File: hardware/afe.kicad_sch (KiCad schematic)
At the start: 36 parts, among them J2 Conn_01x02_Pin, U2 MCP6002-xMC, U3 4052

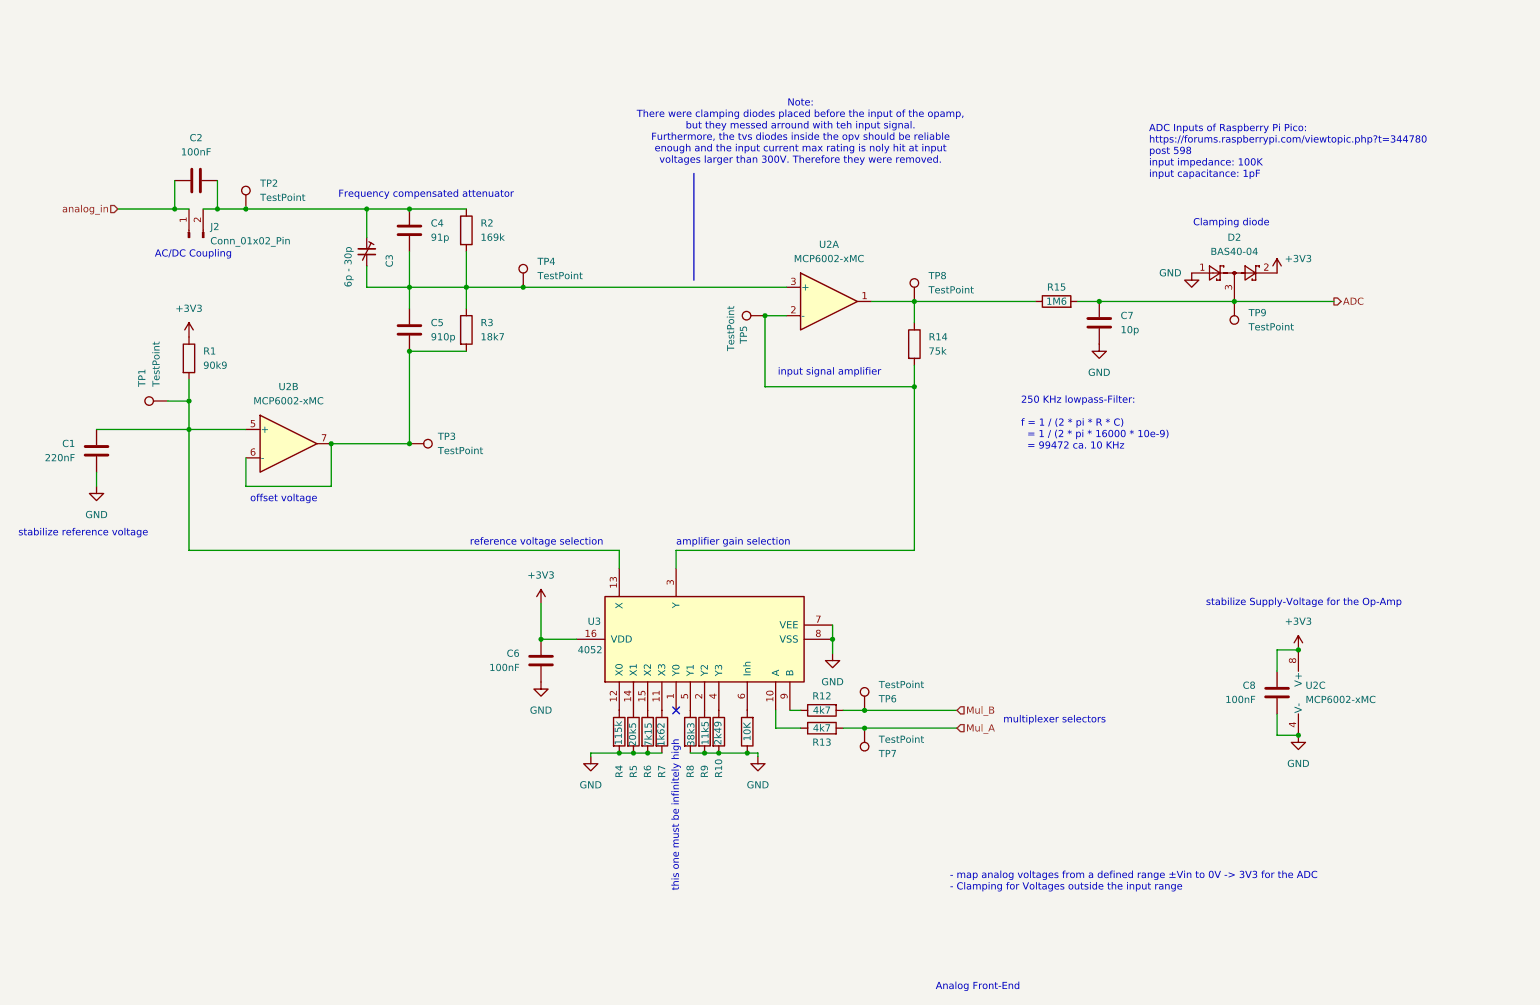
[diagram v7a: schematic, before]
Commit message: remove clamping diodes completely
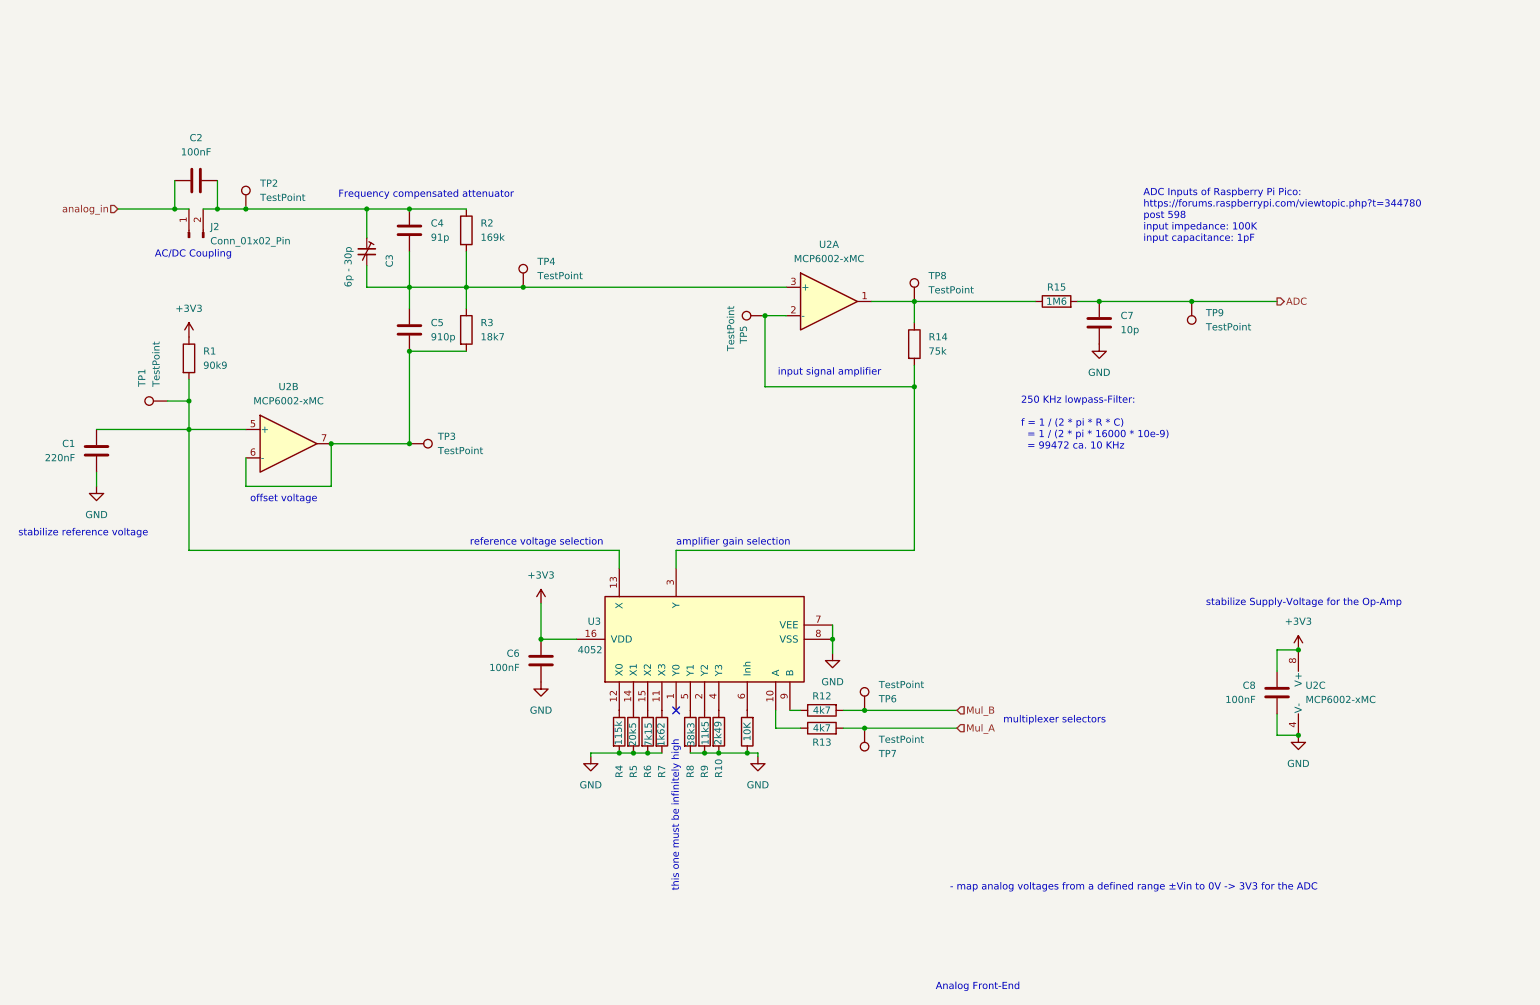
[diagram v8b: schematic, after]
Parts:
- removed D2: BAS40-04, Package_TO_SOT_SMD:SOT-23, symbol Diode:BAS40-04
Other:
- note added: "- map analog voltages from a defined range ±Vin to 0V -> 3V3 for the ADC"
- note removed: "- map analog voltages from a defined range ±Vin to 0V -> 3V3 for the ADC - Clamping for Voltages outside the input range"
- note removed: "Clamping diode"
- note removed: "Note: There were clamping diodes placed before the input of the opamp, but they messed arround with teh input signal. Furthermore, the tvs diodes inside the opv should be reliable enough and the input current max rating is noly hit at input voltages larger than 300V. Therefore they were removed."
- moved on the sheet: TP9
